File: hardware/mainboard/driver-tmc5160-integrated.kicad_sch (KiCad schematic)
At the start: 35 parts, among them M6 Micro-Fit 3.0, U1 TMC5160A-TA

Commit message: redoing board for version alpha 0.2
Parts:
- removed C14: 1μF 63V, Capacitor_SMD:C_1206_3216Metric, symbol Device:C_Small
- removed QA1, QB1: DMHT6016LFJ, corevus:V-DFN5045-12-Type-B, symbol tmc5160-driver:DMHT6016LFJ
- removed R10, R11, R12, R13, R17, R18, R5, R6: 10Ω, AlphaLib:0402R, symbol Device:R_Small
- removed R14, R15: 47Ω, AlphaLib:0402R, symbol Device:R_Small
- removed R16: 33mΩ, Resistor_SMD:R_1206_3216Metric, symbol Device:R
- added C13: 1μF 63V, Capacitor_SMD:C_1206_3216Metric, symbol Device:C_Small
- added Q10, Q11, Q4, Q5, Q6, Q7, Q8, Q9: DMT6016LFDF, corevus:DMT6016LFDF, symbol corevus:DMT6016LFDF-7
- added R7, R8: 47Ω, AlphaLib:0402R, symbol Device:R_Small
- added R9: 33mΩ, Resistor_SMD:R_1206_3216Metric, symbol Device:R
- M6: footprint Connector_Molex:Molex_Micro-Fit_3.0_43650-0400_1x04_P3.00mm_Horizontal -> corevus:XKB_X3025WRS-04C
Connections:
- net GND: now also C13.2, R8.1, R9.2
- net HA1: now also Q6.3 (G)
- net HA2: now also Q4.3 (G)
- net HB1: now also Q10.3 (G)
- net HB2: now also Q8.3 (G)
- net LA1: now also Q7.3 (G)
- net LA2: now also Q5.3 (G)
- net LB1: now also Q11.3 (G)
- net LB2: now also Q9.3 (G)
- net Motor_A1: now also Q6.4 (S), Q6.7 (S), Q7.1 (D), Q7.2 (D), Q7.5 (D), Q7.6 (D), Q7.8 (D)
- net Motor_A2: now also Q4.4 (S), Q4.7 (S), Q5.1 (D), Q5.2 (D), Q5.5 (D), Q5.6 (D), Q5.8 (D)
- net Motor_B1: now also Q10.4 (S), Q10.7 (S), Q11.1 (D), Q11.2 (D), Q11.5 (D), Q11.6 (D), Q11.8 (D)
- net Motor_B2: now also Q8.4 (S), Q8.7 (S), Q9.1 (D), Q9.2 (D), Q9.5 (D), Q9.6 (D), Q9.8 (D)
- net SRBH: now also R7.2
- net SRBL: now also R8.2
- net VM: now also C13.1, Q10.1 (D), Q10.2 (D), Q10.5 (D), Q10.6 (D), Q10.8 (D), Q4.1 (D), Q4.2 (D), Q4.5 (D), Q4.6 (D), Q4.8 (D), Q6.1 (D), Q6.2 (D), Q6.5 (D), Q6.6 (D), Q6.8 (D), Q8.1 (D), Q8.2 (D), Q8.5 (D), Q8.6 (D), Q8.8 (D)
- net at R7.1, R9.1: now also Q5.4 (S), Q5.7 (S), Q7.4 (S), Q7.7 (S)
- new net: Q11.4 (S), Q11.7 (S), Q9.4 (S), Q9.7 (S), R7.1, R9.1
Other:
- moved on the sheet: C13, R7, R8, R9

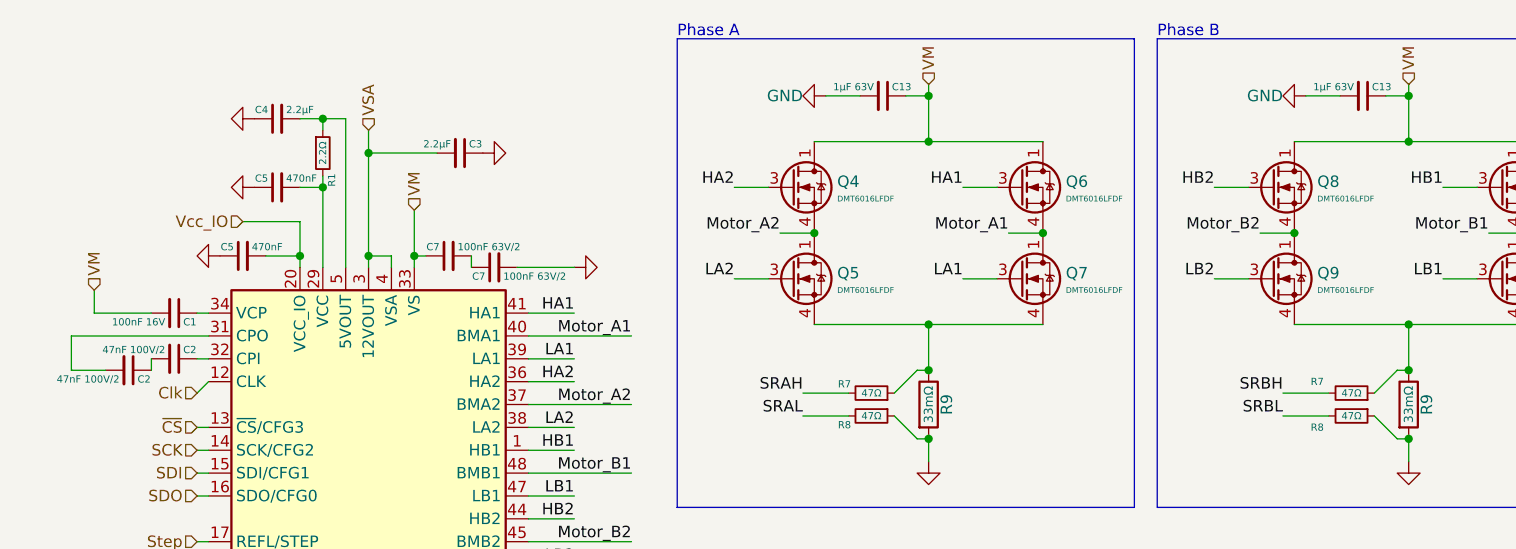
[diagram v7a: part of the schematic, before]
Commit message: added components and further work on PCB layout design
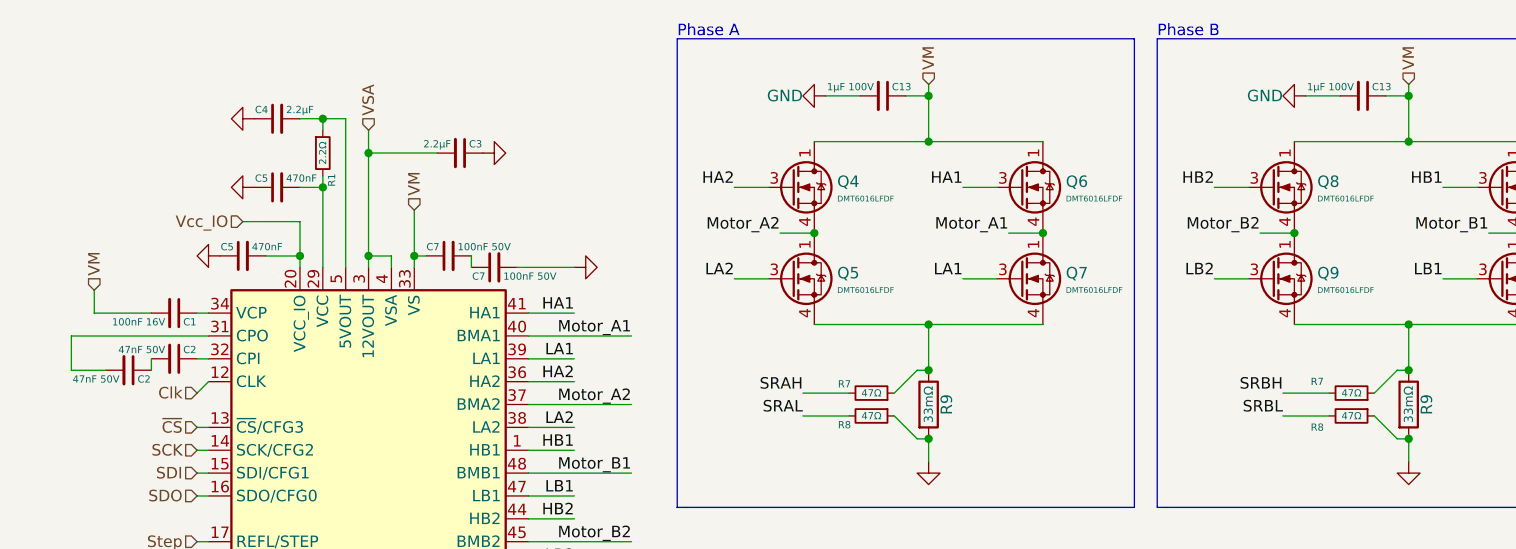
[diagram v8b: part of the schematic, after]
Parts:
- C13: value 1μF 63V -> 1μF 100V
- C2: value 47nF 100V/2 -> 47nF 50V
- C7: value 100nF 63V/2 -> 100nF 50V
- U1: footprint Package_QFP:TQFP-48-1EP_7x7mm_P0.5mm_EP5x5mm_ThermalVias -> corevus:TMCx160
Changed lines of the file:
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@@
       (effects (font (size 0.8 0.8)) (justify left))
     )
-    (property "Value" "47nF 100V/2" (at 33.29 49.8 90)
+    (property "Value" "47nF 50V" (at 33.29 49.8 90)
       (effects (font (size 0.8 0.8)) (justify right))
     )
@@
       (effects (font (size 0.8 0.8)) (justify left))
     )
-    (property "Value" "47nF 100V/2" (at 28.21 53.07 90)
+    (property "Value" "47nF 50V" (at 28.21 53.07 90)
       (effects (font (size 0.8 0.8)) (justify right))
     )
@@
       (effects (font (size 0.8 0.8)) (justify left))
     )
-    (property "Value" "100nF 63V/2" (at 65.77 38.37 90)
+    (property "Value" "100nF 50V" (at 65.77 38.37 90)
       (effects (font (size 0.8 0.8)) (justify right))
     )
@@
       (effects (font (size 1.27 1.27)) (justify left))
     )
-    (property "Footprint" "Package_QFP:TQFP-48-1EP_7x7mm_P0.5mm_EP5x5mm_ThermalVias" (at 55.88 129.54 0)
+    (property "Footprint" "corevus:TMCx160" (at 55.88 129.54 0)
       (effects (font (size 1.27 1.27)) hide)
     )
@@
       (effects (font (size 0.8 0.8)) (justify left))
     )
-    (property "Value" "1μF 63V" (at 165.37 20.59 90)
+    (property "Value" "1μF 100V" (at 165.37 20.59 90)
       (effects (font (size 0.8 0.8)) (justify right))
     )
@@
       (effects (font (size 0.8 0.8)) (justify left))
     )
-    (property "Value" "100nF 63V/2" (at 70.85 41.64 90)
+    (property "Value" "100nF 50V" (at 70.85 41.64 90)
       (effects (font (size 0.8 0.8)) (justify right))
     )
@@
       (effects (font (size 0.8 0.8)) (justify left))
     )
-    (property "Value" "1μF 63V" (at 112.03 20.59 90)
+    (property "Value" "1μF 100V" (at 112.03 20.59 90)
       (effects (font (size 0.8 0.8)) (justify right))
     )
